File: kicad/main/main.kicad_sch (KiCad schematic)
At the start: 7 parts, among them J1 Conn_01x14, J2 Conn_01x14_Socket, J3 Conn_01x04, J4 Conn_01x03_Socket, J7 Conn_01x07, J8 Conn_01x09

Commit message: renamed:    kicad/hoverdeck2/hoverdeck2.kicad_pcb -> attic/kicad/hoverdeck2/hoverdeck2.kicad_pcb
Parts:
- added J5: Conn_01x06, Connector_PinSocket_2.00mm:PinSocket_1x06_P2.00mm_Vertical, symbol Connector_Generic:Conn_01x06
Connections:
- net GND: now also J5.1 (Pin_1)
- net M1: now also J5.3 (Pin_3)
- net M2: now also J5.4 (Pin_4)
- net M3: now also J5.5 (Pin_5)
- net M4: now also J5.6 (Pin_6)
- net VBAT: now also J5.2 (Pin_2)
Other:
- note added: "ESC"
- note added: "REC"
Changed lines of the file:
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@@
 	(generator_version "9.0")
 	(paper "A4")
+	(text "REC"
+		(exclude_from_sim no)
+		(at 154.178 153.162 0)
+		(effects
+			(font
+				(size 1.27 1.27)
+			)
+		)
+	)
+	(text "ESC"
+		(exclude_from_sim no)
+		(at 175.006 133.604 0)
+		(effects
+			(font
+				(size 1.27 1.27)
+			)
+		)
+	)
 	(text "REG"
 		(exclude_from_sim no)
@@
 	(wire
 		(pts
+			(xy 170.18 127) (xy 175.26 127)
+		)
+		(stroke
+			(width 0)
+			(type default)
+		)
+	)
+	(wire
+		(pts
 			(xy 91.44 129.54) (xy 96.52 129.54)
 		)
@@
 	(wire
 		(pts
+			(xy 170.18 124.46) (xy 175.26 124.46)
+		)
+		(stroke
+			(width 0)
+			(type default)
+		)
+	)
+	(wire
+		(pts
 			(xy 119.38 101.6) (xy 124.46 101.6)
 		)
@@
 	(wire
 		(pts
+			(xy 170.18 116.84) (xy 175.26 116.84)
+		)
+		(stroke
+			(width 0)
+			(type default)
+		)
+	)
+	(wire
+		(pts
+			(xy 170.18 121.92) (xy 175.26 121.92)
+		)
+		(stroke
+			(width 0)
+			(type default)
+		)
+	)
+	(wire
+		(pts
 			(xy 114.3 151.13) (xy 119.38 151.13)
 		)
@@
 	(wire
 		(pts
+			(xy 170.18 119.38) (xy 175.26 119.38)
+		)
+		(stroke
+			(width 0)
+			(type default)
+		)
+	)
+	(wire
+		(pts
 			(xy 149.86 144.78) (xy 154.94 144.78)
 		)
@@
 		(pts
 			(xy 142.24 120.65) (xy 147.32 120.65)
+		)
+		(stroke
+			(width 0)
+			(type default)
+		)
+	)
+	(wire
+		(pts
+			(xy 170.18 129.54) (xy 175.26 129.54)
 		)
 		(stroke
@@
 		)
 	)
+	(label "M4"
+		(at 171.45 129.54 0)
+		(effects
+			(font
+				(size 1.27 1.27)
+			)
+			(justify left bottom)
+		)
+	)
 	(label "TX5"
 		(at 119.38 114.3 0)
@@
 		)
 	)
+	(label "M3"
+		(at 171.45 127 0)
+		(effects
+			(font
+				(size 1.27 1.27)
+			)
+			(justify left bottom)
+		)
+	)
 	(label "GND"
 		(at 151.13 142.24 0)
@@
 		)
 	)
+	(label "VBAT"
+		(at 171.45 119.38 0)
+		(effects
+			(font
+				(size 1.27 1.27)
+			)
+			(justify left bottom)
+		)
+	)
 	(label "5V"
 		(at 143.51 115.57 0)
@@
 		)
 	)
+	(label "M1"
+		(at 171.45 121.92 0)
+		(effects
+			(font
+				(size 1.27 1.27)
+			)
+			(justify left bottom)
+		)
+	)
 	(label "M3"
 		(at 92.71 111.76 0)
@@
 		)
 	)
+	(label "M2"
+		(at 171.45 124.46 0)
+		(effects
+			(font
+				(size 1.27 1.27)
+			)
+			(justify left bottom)
+		)
+	)
 	(label "SCL0"
 		(at 114.3 148.59 0)
@@
 		)
 	)
+	(label "GND"
+		(at 171.45 116.84 0)
+		(effects
+			(font
+				(size 1.27 1.27)
+			)
+			(justify left bottom)
+		)
+	)
 	(label "3V3"
 		(at 114.3 158.75 0)
@@
 		)
 	)
+	(symbol
+		(lib_id "Connector_Generic:Conn_01x06")
+		(at 180.34 121.92 0)
+		(unit 1)
+		(exclude_from_sim no)
+		(in_bom yes)
+		(on_board yes)
+		(dnp no)
+		(fields_autoplaced yes)
+		(property "Reference" "J5"
+			(at 182.88 121.9199 0)
+			(effects
+				(font
+					(size 1.27 1.27)
+				)
+				(justify left)
+				(hide yes)
+			)
+		)
+		(property "Value" "Conn_01x06"
+			(at 182.88 124.4599 0)
+			(effects
+				(font
+					(size 1.27 1.27)
+				)
+				(justify left)
+				(hide yes)
+			)
+		)
+		(property "Footprint" "Connector_PinSocket_2.00mm:PinSocket_1x06_P2.00mm_Vertical"
+			(at 180.34 121.92 0)
+			(effects
+				(font
+					(size 1.27 1.27)
+				)
+				(hide yes)
+			)
+		)
+		(property "Datasheet" "~"
+			(at 180.34 121.92 0)
+			(effects
+				(font
+					(size 1.27 1.27)
+				)
+				(hide yes)
+			)
+		)
+		(property "Description" "Generic connector, single row, 01x06, script generated (kicad-library-utils/schlib/autogen/connector/)"
+			(at 180.34 121.92 0)
+			(effects
+				(font
+					(size 1.27 1.27)
+				)
+				(hide yes)
+			)
+		)
+		(pin "2"
+		)
+		(pin "3"
+		)
+		(pin "1"
+		)
+		(pin "4"
+		)
+		(pin "5"
+		)
+		(pin "6"
+		)
+		(instances
+			(project ""
+				(path "/2b1f0318-b347-4cb8-9bbf-78e69ec66761"
+					(reference "J5")
+					(unit 1)
+				)
+			)
+		)
+	)

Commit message: modified:   kicad/main/main.kicad_pcb
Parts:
- added D1: LED, LED_THT:LED_D3.0mm_FlatTop, symbol Device:LED
- added R1: R, Resistor_THT:R_Axial_DIN0204_L3.6mm_D1.6mm_P5.08mm_Horizontal, symbol Device:R
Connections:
- net GND: now also D1.1 (K)
- net LED: now reaches J1.11 (Pin_11)
- net LED: now also R1.2
- new net: D1.2 (A), R1.1
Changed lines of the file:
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@@
+	(wire
+		(pts
+			(xy 144.78 78.74) (xy 149.86 78.74)
+		)
+		(stroke
+			(width 0)
+			(type default)
+		)
+	)
 	(wire
 		(pts
@@
 	(wire
 		(pts
+			(xy 91.44 124.46) (xy 96.52 124.46)
+		)
+		(stroke
+			(width 0)
+			(type default)
+		)
+	)
+	(wire
+		(pts
 			(xy 114.3 158.75) (xy 119.38 158.75)
 		)
@@
 	(wire
 		(pts
+			(xy 157.48 78.74) (xy 161.29 78.74)
+		)
+		(stroke
+			(width 0)
+			(type default)
+		)
+	)
+	(wire
+		(pts
 			(xy 91.44 106.68) (xy 96.52 106.68)
 		)
@@
 	(wire
 		(pts
+			(xy 168.91 78.74) (xy 173.99 78.74)
+		)
+		(stroke
+			(width 0)
+			(type default)
+		)
+	)
+	(wire
+		(pts
 			(xy 119.38 124.46) (xy 124.46 124.46)
 		)
@@
 			(width 0)
 			(type default)
+		)
+	)
+	(label "LED"
+		(at 91.44 124.46 0)
+		(effects
+			(font
+				(size 1.27 1.27)
+			)
+			(justify left bottom)
 		)
 	)
@@
 		)
 	)
+	(label "GND"
+		(at 146.05 78.74 0)
+		(effects
+			(font
+				(size 1.27 1.27)
+			)
+			(justify left bottom)
+		)
+	)
 	(label "SDA0"
 		(at 114.3 153.67 0)
@@
 		)
 	)
+	(label "LED"
+		(at 168.91 78.74 0)
+		(effects
+			(font
+				(size 1.27 1.27)
+			)
+			(justify left bottom)
+		)
+	)
 	(label "TX5"
 		(at 151.13 149.86 0)
@@
 			)
 			(justify left bottom)
+		)
+	)
+	(symbol
+		(lib_id "Device:LED")
+		(at 153.67 78.74 0)
+		(unit 1)
+		(exclude_from_sim no)
+		(in_bom yes)
+		(on_board yes)
+		(dnp no)
+		(fields_autoplaced yes)
+		(property "Reference" "D1"
+			(at 152.0825 72.39 0)
+			(effects
+				(font
+					(size 1.27 1.27)
+				)
+				(hide yes)
+			)
+		)
+		(property "Value" "LED"
+			(at 152.0825 74.93 0)
+			(effects
+				(font
+					(size 1.27 1.27)
+				)
+			)
+		)
+		(property "Footprint" "LED_THT:LED_D3.0mm_FlatTop"
+			(at 153.67 78.74 0)
+			(effects
+				(font
+					(size 1.27 1.27)
+				)
+				(hide yes)
+			)
+		)
+		(property "Datasheet" "~"
+			(at 153.67 78.74 0)
+			(effects
+				(font
+					(size 1.27 1.27)
+				)
+				(hide yes)
+			)
+		)
+		(property "Description" "Light emitting diode"
+			(at 153.67 78.74 0)
+			(effects
+				(font
+					(size 1.27 1.27)
+				)
+				(hide yes)
+			)
+		)
+		(property "Sim.Pins" "1=K 2=A"
+			(at 153.67 78.74 0)
+			(effects
+				(font
+					(size 1.27 1.27)
+				)
+				(hide yes)
+			)
+		)
+		(pin "2"
+		)
+		(pin "1"
+		)
+		(instances
+			(project "main"
+				(path "/2b1f0318-b347-4cb8-9bbf-78e69ec66761"
+					(reference "D1")
+					(unit 1)
+				)
+			)
 		)
 	)
@@
 					(unit 1)
 				)
+			)
+		)
+	)
+	(symbol
+		(lib_id "Device:R")
+		(at 165.1 78.74 90)
+		(unit 1)
+		(exclude_from_sim no)
+		(in_bom yes)
+		(on_board yes)
+		(dnp no)
+		(fields_autoplaced yes)
+		(property "Reference" "R1"
+			(at 165.1 72.39 90)
+			(effects
+				(font
+					(size 1.27 1.27)
+				)
+				(hide yes)
+			)
+		)
+		(property "Value" "R"
+			(at 165.1 74.93 90)
+			(effects
+				(font
+					(size 1.27 1.27)
+				)
+			)
+		)
+		(property "Footprint" "Resistor_THT:R_Axial_DIN0204_L3.6mm_D1.6mm_P5.08mm_Horizontal"
+			(at 165.1 80.518 90)
+			(effects
+				(font
+					(size 1.27 1.27)
+				)
+				(hide yes)
+			)
+		)
+		(property "Datasheet" "~"
+			(at 165.1 78.74 0)
+			(effects
+				(font
+					(size 1.27 1.27)
+				)
+				(hide yes)
+			)
+		)
+		(property "Description" "Resistor"
+			(at 165.1 78.74 0)
+			(effects
+				(font
+					(size 1.27 1.27)
+				)
+				(hide yes)
+			)
+		)
+		(pin "1"
+		)
+		(pin "2"
+		)
+		(instances
+			(project "main"
+				(path "/2b1f0318-b347-4cb8-9bbf-78e69ec66761"
+					(reference "R1")
+					(unit 1)
+				)

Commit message: modified:   kicad/main/main.kicad_pcb
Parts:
- added J6: Conn_01x08, Connector_PinSocket_2.00mm:PinSocket_1x08_P2.00mm_Vertical, symbol Connector_Generic:Conn_01x08
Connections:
- net 3V3: now also J6.8 (Pin_8)
- net CS: now also J6.4 (Pin_4)
- net GND: now also J6.7 (Pin_7)
- net MISO: now also J6.2 (Pin_2)
- net MOSI: now also J6.3 (Pin_3)
- net SCK: now also J6.1 (Pin_1)
- net SCL1: now also J6.5 (Pin_5)
- net SDA1: now also J6.6 (Pin_6)
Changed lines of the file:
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@@
+	(wire
+		(pts
+			(xy 50.8 120.65) (xy 54.61 120.65)
+		)
+		(stroke
+			(width 0)
+			(type default)
+		)
+	)
 	(wire
 		(pts
@@
 	(wire
 		(pts
+			(xy 50.8 123.19) (xy 54.61 123.19)
+		)
+		(stroke
+			(width 0)
+			(type default)
+		)
+	)
+	(wire
+		(pts
 			(xy 91.44 114.3) (xy 96.52 114.3)
 		)
@@
 	(wire
 		(pts
+			(xy 50.8 125.73) (xy 54.61 125.73)
+		)
+		(stroke
+			(width 0)
+			(type default)
+		)
+	)
+	(wire
+		(pts
 			(xy 142.24 118.11) (xy 147.32 118.11)
 		)
@@
 	(wire
 		(pts
+			(xy 50.8 130.81) (xy 54.61 130.81)
+		)
+		(stroke
+			(width 0)
+			(type default)
+		)
+	)
+	(wire
+		(pts
 			(xy 170.18 127) (xy 175.26 127)
 		)
@@
 	(wire
 		(pts
+			(xy 50.8 133.35) (xy 54.61 133.35)
+		)
+		(stroke
+			(width 0)
+			(type default)
+		)
+	)
+	(wire
+		(pts
 			(xy 170.18 124.46) (xy 175.26 124.46)
 		)
@@
 	(wire
 		(pts
+			(xy 50.8 135.89) (xy 54.61 135.89)
+		)
+		(stroke
+			(width 0)
+			(type default)
+		)
+	)
+	(wire
+		(pts
 			(xy 114.3 151.13) (xy 119.38 151.13)
 		)
@@
 	(wire
 		(pts
+			(xy 50.8 138.43) (xy 54.61 138.43)
+		)
+		(stroke
+			(width 0)
+			(type default)
+		)
+	)
+	(wire
+		(pts
 			(xy 114.3 148.59) (xy 119.38 148.59)
 		)
@@
 		(pts
 			(xy 91.44 99.06) (xy 96.52 99.06)
+		)
+		(stroke
+			(width 0)
+			(type default)
+		)
+	)
+	(wire
+		(pts
+			(xy 50.8 128.27) (xy 54.61 128.27)
 		)
 		(stroke
@@
 		)
 	)
+	(label "MISO"
+		(at 50.8 123.19 0)
+		(effects
+			(font
+				(size 1.27 1.27)
+			)
+			(justify left bottom)
+		)
+	)
 	(label "RX5"
 		(at 119.38 111.76 0)
@@
 		)
 	)
+	(label "SCK"
+		(at 50.8 120.65 0)
+		(effects
+			(font
+				(size 1.27 1.27)
+			)
+			(justify left bottom)
+		)
+	)
 	(label "MISO"
 		(at 91.44 132.08 0)
@@
 		)
 	)
+	(label "SDA1"
+		(at 50.8 133.35 0)
+		(effects
+			(font
+				(size 1.27 1.27)
+			)
+			(justify left bottom)
+		)
+	)
 	(label "M2"
 		(at 171.45 124.46 0)
@@
 		)
 	)
+	(label "3V3"
+		(at 50.8 138.43 0)
+		(effects
+			(font
+				(size 1.27 1.27)
+			)
+			(justify left bottom)
+		)
+	)
+	(label "MOSI"
+		(at 50.8 125.73 0)
+		(effects
+			(font
+				(size 1.27 1.27)
+			)
+			(justify left bottom)
+		)
+	)
 	(label "GND"
 		(at 143.51 118.11 0)
@@
 		)
 	)
+	(label "CS"
+		(at 50.8 128.27 0)
+		(effects
+			(font
+				(size 1.27 1.27)
+			)
+			(justify left bottom)
+		)
+	)
 	(label "GND"
 		(at 86.36 153.67 0)
@@
 		)
 	)
+	(label "SCL1"
+		(at 50.8 130.81 0)
+		(effects
+			(font
+				(size 1.27 1.27)
+			)
+			(justify left bottom)
+		)
+	)
 	(label "TX5"
 		(at 151.13 149.86 0)
+		(effects
+			(font
+				(size 1.27 1.27)
+			)
+			(justify left bottom)
+		)
+	)
+	(label "GND"
+		(at 50.8 135.89 0)
 		(effects
 			(font
@@
 					(unit 1)
 				)
+			)
+		)
+	)
+	(symbol
+		(lib_id "Connector_Generic:Conn_01x08")
+		(at 59.69 128.27 0)
+		(unit 1)
+		(exclude_from_sim no)
+		(in_bom yes)
+		(on_board yes)
+		(dnp no)
+		(fields_autoplaced yes)
+		(property "Reference" "J6"
+			(at 62.23 128.2699 0)
+			(effects
+				(font
+					(size 1.27 1.27)
+				)
+				(justify left)
+				(hide yes)
+			)
+		)
+		(property "Value" "Conn_01x08"
+			(at 62.23 130.8099 0)
+			(effects
+				(font
+					(size 1.27 1.27)
+				)
+				(justify left)
+				(hide yes)
+			)
+		)
+		(property "Footprint" "Connector_PinSocket_2.00mm:PinSocket_1x08_P2.00mm_Vertical"
+			(at 59.69 128.27 0)
+			(effects
+				(font
+					(size 1.27 1.27)
+				)
+				(hide yes)
+			)
+		)
+		(property "Datasheet" "~"
+			(at 59.69 128.27 0)
+			(effects
+				(font
+					(size 1.27 1.27)
+				)
+				(hide yes)
+			)
+		)
+		(property "Description" "Generic connector, single row, 01x08, script generated (kicad-library-utils/schlib/autogen/connector/)"
+			(at 59.69 128.27 0)
+			(effects
+				(font
+					(size 1.27 1.27)
+				)
+				(hide yes)
+			)
+		)
+		(pin "3"
+		)
+		(pin "4"
+		)
+		(pin "1"
+		)
+		(pin "2"
+		)
+		(pin "5"
+		)
+		(pin "6"
+		)
+		(pin "8"
+		)
+		(pin "7"
+		)
+		(instances
+			(project ""
+				(path "/2b1f0318-b347-4cb8-9bbf-78e69ec66761"
+					(reference "J6")
+					(unit 1)
+				)

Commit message: modified:   kicad/main/main.kicad_pcb
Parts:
- removed J3: Conn_01x04, Connector_PinHeader_2.00mm:PinHeader_1x04_P2.00mm_Vertical, symbol Connector_Generic:Conn_01x04
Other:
- note removed: "REC"
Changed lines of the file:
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@@
 	(generator_version "9.0")
 	(paper "A4")
-	(text "REC"
-		(exclude_from_sim no)
-		(at 154.178 153.162 0)
-		(effects
-			(font
-				(size 1.27 1.27)
-			)
-		)
-	)
 	(text "ESC"
 		(exclude_from_sim no)
@@
 	(wire
 		(pts
-			(xy 149.86 147.32) (xy 154.94 147.32)
-		)
-		(stroke
-			(width 0)
-			(type default)
-		)
-	)
-	(wire
-		(pts
 			(xy 168.91 78.74) (xy 173.99 78.74)
 		)
@@
 	(wire
 		(pts
-			(xy 149.86 142.24) (xy 154.94 142.24)
-		)
-		(stroke
-			(width 0)
-			(type default)
-		)
-	)
-	(wire
-		(pts
 			(xy 170.18 119.38) (xy 175.26 119.38)
 		)
@@
 	(wire
 		(pts
-			(xy 149.86 144.78) (xy 154.94 144.78)
-		)
-		(stroke
-			(width 0)
-			(type default)
-		)
-	)
-	(wire
-		(pts
 			(xy 91.44 132.08) (xy 96.52 132.08)
 		)
@@
 		(pts
 			(xy 50.8 128.27) (xy 54.61 128.27)
-		)
-		(stroke
-			(width 0)
-			(type default)
-		)
-	)
-	(wire
-		(pts
-			(xy 149.86 149.86) (xy 154.94 149.86)
 		)
 		(stroke
@@
 	)
 	(label "GND"
-		(at 151.13 142.24 0)
-		(effects
-			(font
-				(size 1.27 1.27)
-			)
-			(justify left bottom)
-		)
-	)
-	(label "GND"
 		(at 120.65 101.6 0)
 		(effects
@@
 		)
 	)
-	(label "RX5"
-		(at 151.13 147.32 0)
-		(effects
-			(font
-				(size 1.27 1.27)
-			)
-			(justify left bottom)
-		)
-	)
 	(label "3V3"
 		(at 50.8 138.43 0)
@@
 		)
 	)
-	(label "5V"
-		(at 151.13 144.78 0)
-		(effects
-			(font
-				(size 1.27 1.27)
-			)
-			(justify left bottom)
-		)
-	)
 	(label "GND"
 		(at 146.05 78.74 0)
@@
 	(label "SCL1"
 		(at 50.8 130.81 0)
-		(effects
-			(font
-				(size 1.27 1.27)
-			)
-			(justify left bottom)
-		)
-	)
-	(label "TX5"
-		(at 151.13 149.86 0)
 		(effects
 			(font
@@
 		)
 		(instances
-			(project ""
+			(project "main"
 				(path "/2b1f0318-b347-4cb8-9bbf-78e69ec66761"
 					(reference "J5")
@@
 		)
 		(instances
-			(project ""
+			(project "main"
 				(path "/2b1f0318-b347-4cb8-9bbf-78e69ec66761"
 					(reference "J6")
@@
 		)
 		(instances
-			(project "teensy2-bottom-bmi088"
+			(project "main"
 				(path "/2b1f0318-b347-4cb8-9bbf-78e69ec66761"
 					(reference "J8")
@@
 		)
 		(instances
-			(project "teensy2-bottom-bmi088"
+			(project "main"
 				(path "/2b1f0318-b347-4cb8-9bbf-78e69ec66761"
 					(reference "J2")
-					(unit 1)
-				)
-			)
-		)
-	)
-	(symbol
-		(lib_id "Connector_Generic:Conn_01x04")
-		(at 160.02 144.78 0)
-		(unit 1)
-		(exclude_from_sim no)
-		(in_bom yes)
-		(on_board yes)
-		(dnp no)
-		(fields_autoplaced yes)
-		(property "Reference" "J3"
-			(at 162.56 144.7799 0)
-			(effects
-				(font
-					(size 1.27 1.27)
-				)
-				(justify left)
-				(hide yes)
-			)
-		)
-		(property "Value" "Conn_01x04"
-			(at 162.56 147.3199 0)
-			(effects
-				(font
-					(size 1.27 1.27)
-				)
-				(justify left)
-				(hide yes)
-			)
-		)
-		(property "Footprint" "Connector_PinHeader_2.00mm:PinHeader_1x04_P2.00mm_Vertical"
-			(at 160.02 144.78 0)
-			(effects
-				(font
-					(size 1.27 1.27)
-				)
-				(hide yes)
-			)
-		)
-		(property "Datasheet" "~"
-			(at 160.02 144.78 0)
-			(effects
-				(font
-					(size 1.27 1.27)
-				)
-				(hide yes)
-			)
-		)
-		(property "Description" "Generic connector, single row, 01x04, script generated (kicad-library-utils/schlib/autogen/connector/)"
-			(at 160.02 144.78 0)
-			(effects
-				(font
-					(size 1.27 1.27)
-				)
-				(hide yes)
-			)
-		)
-		(pin "4"
-		)
-		(pin "2"
-		)
-		(pin "1"
-		)
-		(pin "3"
-		)
-		(instances
-			(project ""
-				(path "/2b1f0318-b347-4cb8-9bbf-78e69ec66761"
-					(reference "J3")
 					(unit 1)
 				)
@@
 		)
 		(instances
-			(project "teensy2-bottom-bmi088"
+			(project "main"
 				(path "/2b1f0318-b347-4cb8-9bbf-78e69ec66761"
 					(reference "J7")
@@
 		)
 		(instances
-			(project "teensy2-bottom-bmi088"
+			(project "main"
 				(path "/2b1f0318-b347-4cb8-9bbf-78e69ec66761"
 					(reference "J1")
@@
 		)
 		(instances
-			(project "teensy2-bottom-bmi088"
+			(project "main"
 				(path "/2b1f0318-b347-4cb8-9bbf-78e69ec66761"
 					(reference "H1")
@@
 		)
 		(instances
-			(project "teensy2-bottom-bmi088"
+			(project "main"
 				(path "/2b1f0318-b347-4cb8-9bbf-78e69ec66761"
 					(reference "J4")

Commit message: modified:   kicad/main/main.kicad_pcb
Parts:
- R1: footprint Resistor_THT:R_Axial_DIN0204_L3.6mm_D1.6mm_P5.08mm_Horizontal -> Resistor_THT:R_Axial_DIN0204_L3.6mm_D1.6mm_P7.62mm_Horizontal
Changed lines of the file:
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@@
 			)
 		)
-		(property "Footprint" "Resistor_THT:R_Axial_DIN0204_L3.6mm_D1.6mm_P5.08mm_Horizontal"
+		(property "Footprint" "Resistor_THT:R_Axial_DIN0204_L3.6mm_D1.6mm_P7.62mm_Horizontal"
 			(at 165.1 80.518 90)
 			(effects

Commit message: modified:   kicad/main/main.kicad_pcb
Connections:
- net RX5: no longer names the net of J2.6 (Pin_6)
- net TX5: no longer names the net of J2.7 (Pin_7)
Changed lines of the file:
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@@
-	(wire
-		(pts
-			(xy 119.38 111.76) (xy 124.46 111.76)
-		)
-		(stroke
-			(width 0)
-			(type default)
-		)
-	)
 	(wire
 		(pts
@@
 		(pts
 			(xy 91.44 106.68) (xy 96.52 106.68)
-		)
-		(stroke
-			(width 0)
-			(type default)
-		)
-	)
-	(wire
-		(pts
-			(xy 119.38 114.3) (xy 124.46 114.3)
 		)
 		(stroke
@@
 		)
 	)
-	(label "RX5"
-		(at 119.38 111.76 0)
-		(effects
-			(font
-				(size 1.27 1.27)
-			)
-			(justify left bottom)
-		)
-	)
 	(label "SDA0"
 		(at 119.38 119.38 0)
@@
 		(effects
 			(font
-				(size 1.27 1.27)
-			)
-			(justify left bottom)
-		)
-	)
-	(label "TX5"
-		(at 119.38 114.3 0)
-		(effects
-			(font

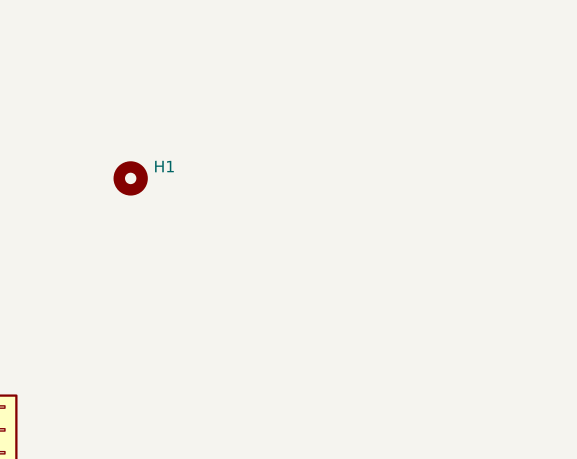
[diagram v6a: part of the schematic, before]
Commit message: Schematic has separate component for each hole
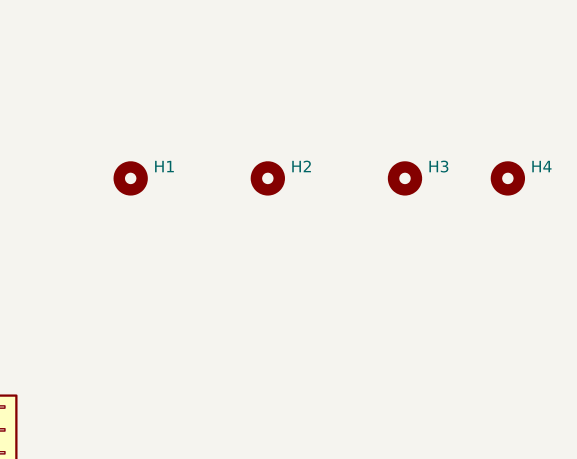
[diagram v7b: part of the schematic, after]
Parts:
- added H2, H3, H4: MountingHole, MountingHole:MountingHole_2.5mm, symbol Mechanical:MountingHole
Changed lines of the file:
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@@
+	)
+	(symbol
+		(lib_id "Mechanical:MountingHole")
+		(at 209.55 91.44 0)
+		(unit 1)
+		(exclude_from_sim no)
+		(in_bom no)
+		(on_board yes)
+		(dnp no)
+		(fields_autoplaced yes)
+		(property "Reference" "H2"
+			(at 212.09 90.1699 0)
+			(effects
+				(font
+					(size 1.27 1.27)
+				)
+				(justify left)
+			)
+		)
+		(property "Value" "MountingHole"
+			(at 212.09 92.7099 0)
+			(effects
+				(font
+					(size 1.27 1.27)
+				)
+				(justify left)
+				(hide yes)
+			)
+		)
+		(property "Footprint" "MountingHole:MountingHole_2.5mm"
+			(at 209.55 91.44 0)
+			(effects
+				(font
+					(size 1.27 1.27)
+				)
+				(hide yes)
+			)
+		)
+		(property "Datasheet" "~"
+			(at 209.55 91.44 0)
+			(effects
+				(font
+					(size 1.27 1.27)
+				)
+				(hide yes)
+			)
+		)
+		(property "Description" "Mounting Hole without connection"
+			(at 209.55 91.44 0)
+			(effects
+				(font
+					(size 1.27 1.27)
+				)
+				(hide yes)
+			)
+		)
+		(instances
+			(project "main"
+				(path "/2b1f0318-b347-4cb8-9bbf-78e69ec66761"
+					(reference "H2")
+					(unit 1)
+				)
+			)
+		)
 	)
 	(symbol
@@
 	)
 	(symbol
+		(lib_id "Mechanical:MountingHole")
+		(at 224.79 91.44 0)
+		(unit 1)
+		(exclude_from_sim no)
+		(in_bom no)
+		(on_board yes)
+		(dnp no)
+		(fields_autoplaced yes)
+		(property "Reference" "H3"
+			(at 227.33 90.1699 0)
+			(effects
+				(font
+					(size 1.27 1.27)
+				)
+				(justify left)
+			)
+		)
+		(property "Value" "MountingHole"
+			(at 227.33 92.7099 0)
+			(effects
+				(font
+					(size 1.27 1.27)
+				)
+				(justify left)
+				(hide yes)
+			)
+		)
+		(property "Footprint" "MountingHole:MountingHole_2.5mm"
+			(at 224.79 91.44 0)
+			(effects
+				(font
+					(size 1.27 1.27)
+				)
+				(hide yes)
+			)
+		)
+		(property "Datasheet" "~"
+			(at 224.79 91.44 0)
+			(effects
+				(font
+					(size 1.27 1.27)
+				)
+				(hide yes)
+			)
+		)
+		(property "Description" "Mounting Hole without connection"
+			(at 224.79 91.44 0)
+			(effects
+				(font
+					(size 1.27 1.27)
+				)
+				(hide yes)
+			)
+		)
+		(instances
+			(project "main"
+				(path "/2b1f0318-b347-4cb8-9bbf-78e69ec66761"
+					(reference "H3")
+					(unit 1)
+				)
+			)
+		)
+	)
+	(symbol
 		(lib_id "Connector_Generic:Conn_01x07")
 		(at 95.25 156.21 0)
@@
 					(unit 1)
 				)
+			)
+		)
+	)
+	(symbol
+		(lib_id "Mechanical:MountingHole")
+		(at 236.22 91.44 0)
+		(unit 1)
+		(exclude_from_sim no)
+		(in_bom no)
+		(on_board yes)
+		(dnp no)
+		(fields_autoplaced yes)
+		(property "Reference" "H4"
+			(at 238.76 90.1699 0)
+			(effects
+				(font
+					(size 1.27 1.27)
+				)
+				(justify left)
+			)
+		)
+		(property "Value" "MountingHole"
+			(at 238.76 92.7099 0)
+			(effects
+				(font
+					(size 1.27 1.27)
+				)
+				(justify left)
+				(hide yes)
+			)
+		)
+		(property "Footprint" "MountingHole:MountingHole_2.5mm"
+			(at 236.22 91.44 0)
+			(effects
+				(font
+					(size 1.27 1.27)
+				)
+				(hide yes)
+			)
+		)
+		(property "Datasheet" "~"
+			(at 236.22 91.44 0)
+			(effects
+				(font
+					(size 1.27 1.27)
+				)
+				(hide yes)
+			)
+		)
+		(property "Description" "Mounting Hole without connection"
+			(at 236.22 91.44 0)
+			(effects
+				(font
+					(size 1.27 1.27)
+				)
+				(hide yes)
+			)
+		)
+		(instances
+			(project "main"
+				(path "/2b1f0318-b347-4cb8-9bbf-78e69ec66761"
+					(reference "H4")
+					(unit 1)
+				)
